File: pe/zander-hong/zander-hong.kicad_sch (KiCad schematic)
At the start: 0 parts

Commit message: corrected file errors and renamed templates to correct names
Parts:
- added C1, C2, C2A, C3: C, symbol Device:C
- added L1: L, symbol Device:L
- added R1, R2: R, symbol Device:R
- added U1: AP62300TWU, Package_TO_SOT_SMD:TSOT-23-6, symbol Regulator_Switching:AP62300TWU
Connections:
- new net: R1.1, R2.1, U1.4 (FB)
- new net: C3.1, L1.2, U1.2 (SW)
- new net: C3.2, U1.6 (BST)
- new net +12V: C1.2, U1.3 (IN), U1.5 (EN)
- new net GND: C1.1, C2.1, C2A.2, R2.2, U1.1 (GND)
- new net Vout: C2.2, C2A.1, L1.1, R1.2
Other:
- note added: "C1: Input Filtering Cap C2 & C2A: Output Filtering Cap in parrallel to account for DC Bias Derating C3: Bootstrap Cap to power gate for N channel MOSFET"
- note added: "R1 & R2: Sample Voltage Output to ensure precise step down"
- company: (none) -> Formula Slug
- title: (none) -> ${BOARD_TITLE}

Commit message: completed PCB and Schematic and fixed some more file errors
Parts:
- C1, C2, C3: footprint (none) -> Capacitor_SMD:C_0603_1608Metric
- C2A1: renamed from C2A; footprint (none) -> Capacitor_SMD:C_0603_1608Metric
- L1: footprint (none) -> Inductor_SMD:L_SRP4020TA
- R1, R2: footprint (none) -> Resistor_SMD:R_0603_1608Metric
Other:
- note added: "C1: Input Filtering Cap C2 & C2A: Output Filtering Cap in parallel to account for DC Bias Derating C3: Bootstrap Cap to power gate for N channel MOSFET"
- note removed: "C1: Input Filtering Cap C2 & C2A: Output Filtering Cap in parrallel to account for DC Bias Derating C3: Bootstrap Cap to power gate for N channel MOSFET"

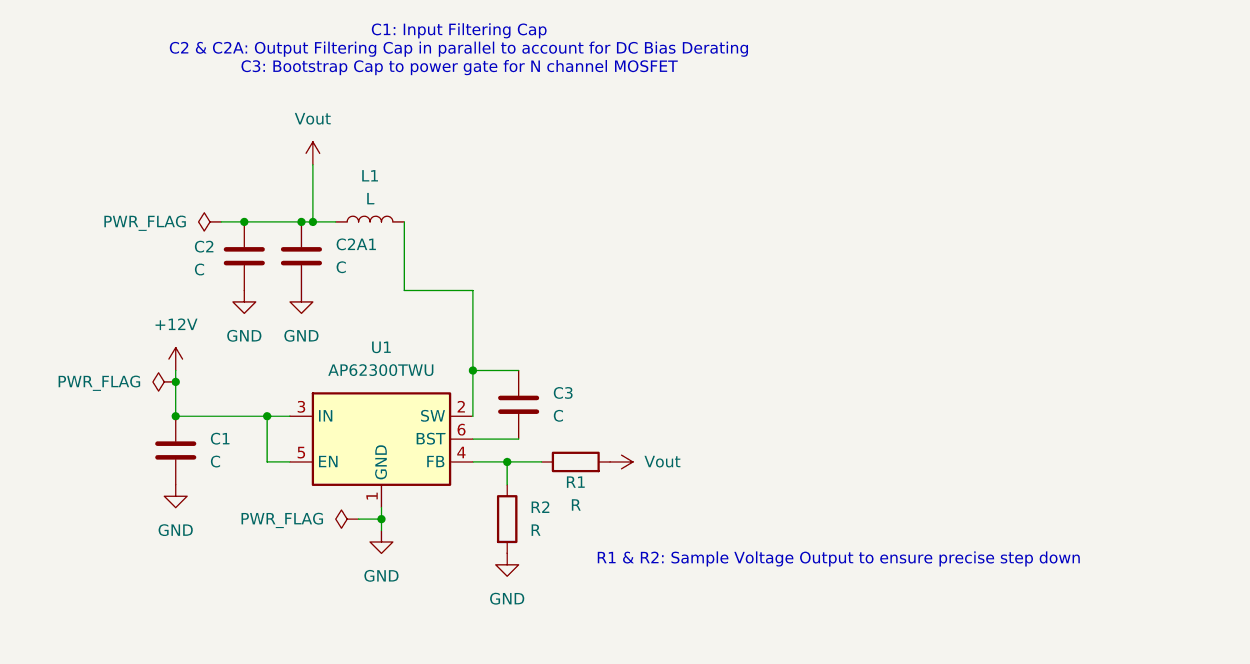
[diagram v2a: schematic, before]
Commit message: changed enable high voltage from 12v to 5v
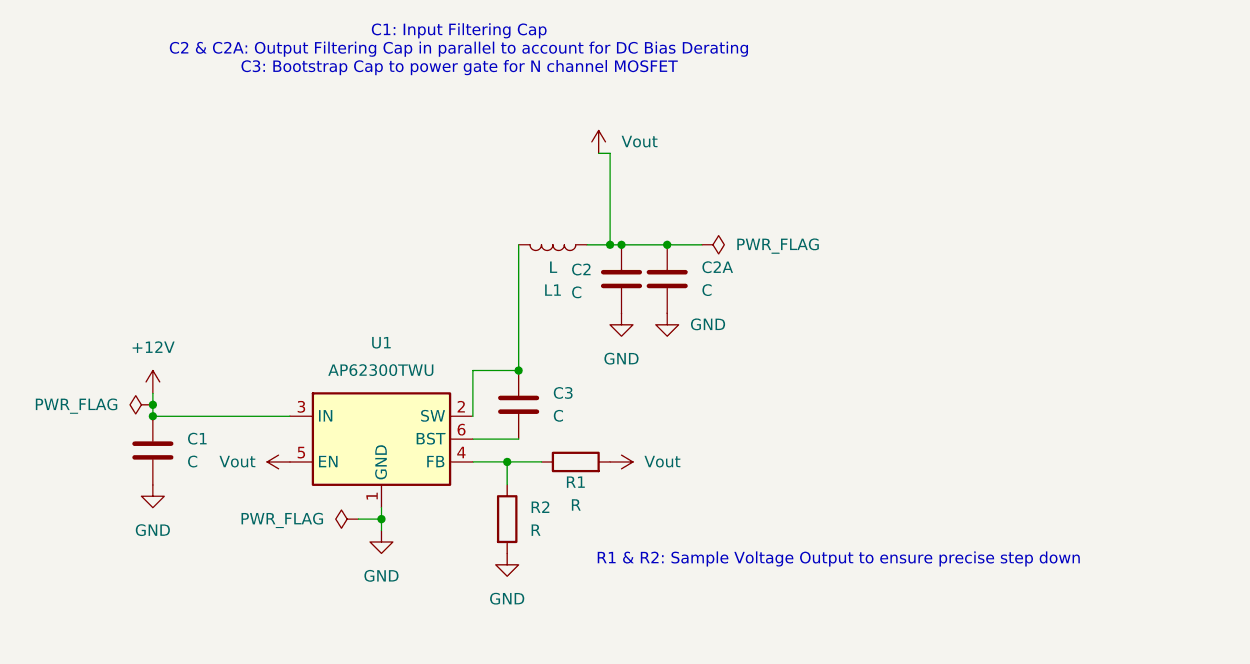
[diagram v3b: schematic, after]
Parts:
- renumbered C2A1 to C2A
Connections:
- net +12V: no longer U1.5 (EN)
- net Vout: now also U1.5 (EN)
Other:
- moved on the sheet: C1, C2, C2A, L1

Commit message: changes in schematic formatting and footprints along with enable no connect
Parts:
- L1: footprint Inductor_SMD:L_SRP4020TA -> inductor_SRP4020:IND_SRP4020_BRN
- renumbered C2A to C2A1
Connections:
- net Vout: no longer U1.5 (EN)
- no-connect marks 0 -> 1
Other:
- note added: "R1 & R2: Voltage divider for FB pin to sample Vout for precise step down"
- note removed: "R1 & R2: Sample Voltage Output to ensure precise step down"
- moved on the sheet: R1, R2
